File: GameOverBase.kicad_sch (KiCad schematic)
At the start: 55 parts, among them J1 USB_C_DEALON-USB-US31-106, J2 Serial Port, J3 add-on conn, Q1 PMN48XP, SW1 SW_DIP_x08, SW2 boot, SW3 Reset, U1 ESP32-WROOM-E, U2 4021, U3 MCP73831-2ACI-OT, U4 XC6210B332MR

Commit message: Reduces mounting holes to M2 size
It's now clear that this difference will be significant in the layout
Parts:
- H1, H2: footprint MountingHole:MountingHole_3.2mm_M3_DIN965_Pad -> (none)
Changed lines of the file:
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@@
       (effects (font (size 1.27 1.27)) (justify left))
     )
-    (property "Footprint" "MountingHole:MountingHole_3.2mm_M3_DIN965_Pad" (id 2) (at 276.86 142.24 0)
+    (property "Footprint" "" (id 2) (at 276.86 142.24 0)
       (effects (font (size 1.27 1.27)) hide)
     )
@@
       (effects (font (size 1.27 1.27)) (justify left))
     )
-    (property "Footprint" "MountingHole:MountingHole_3.2mm_M3_DIN965_Pad" (id 2) (at 266.7 142.24 0)
+    (property "Footprint" "" (id 2) (at 266.7 142.24 0)
       (effects (font (size 1.27 1.27)) hide)
     )
@@
     )
     (path "/72b8070d-6360-4ae2-9e52-c57614a73147"
-      (reference "H1") (unit 1) (value "~") (footprint "MountingHole:MountingHole_3.2mm_M3_DIN965_Pad")
+      (reference "H1") (unit 1) (value "~") (footprint "MountingHole:MountingHole_2.2mm_M2_Pad_Via")
     )
     (path "/33ba6f87-8078-4806-af25-74c46ae2d6bf"
-      (reference "H2") (unit 1) (value "~") (footprint "MountingHole:MountingHole_3.2mm_M3_DIN965_Pad")
+      (reference "H2") (unit 1) (value "~") (footprint "MountingHole:MountingHole_2.2mm_M2_Pad_Via")
     )
     (path "/c62df308-9d46-4880-b5c7-5b78f375875b"

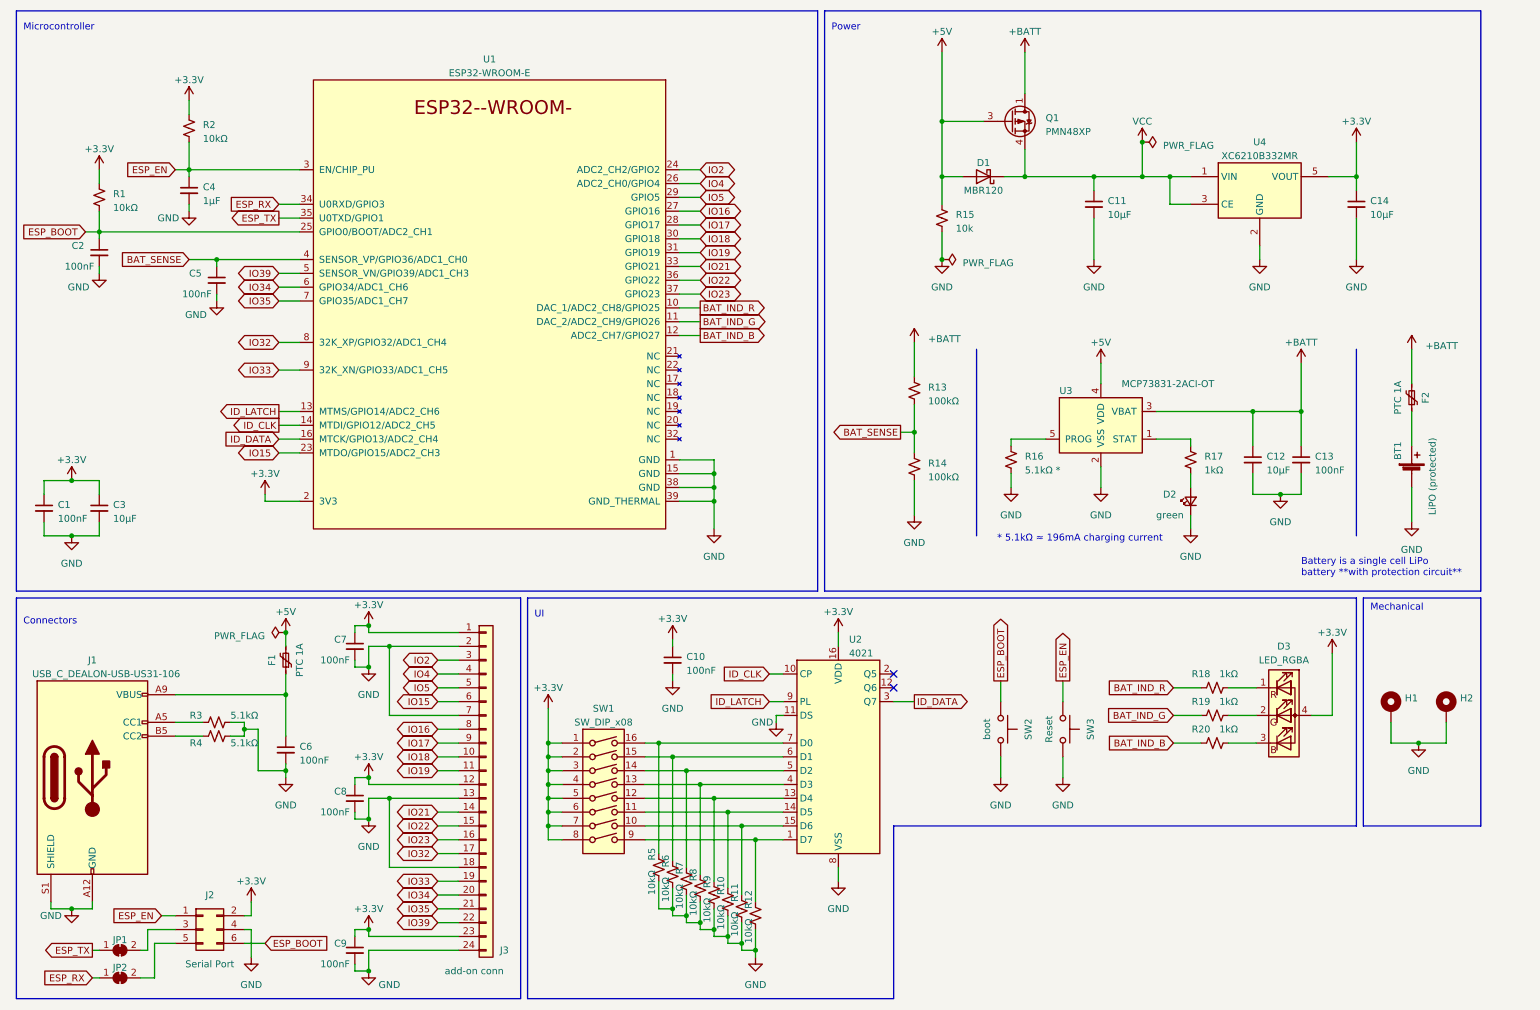
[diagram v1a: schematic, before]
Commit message: Uses a resistor network for the pull-ups in the ID DIP switch
This will save a lot of space on the PCB
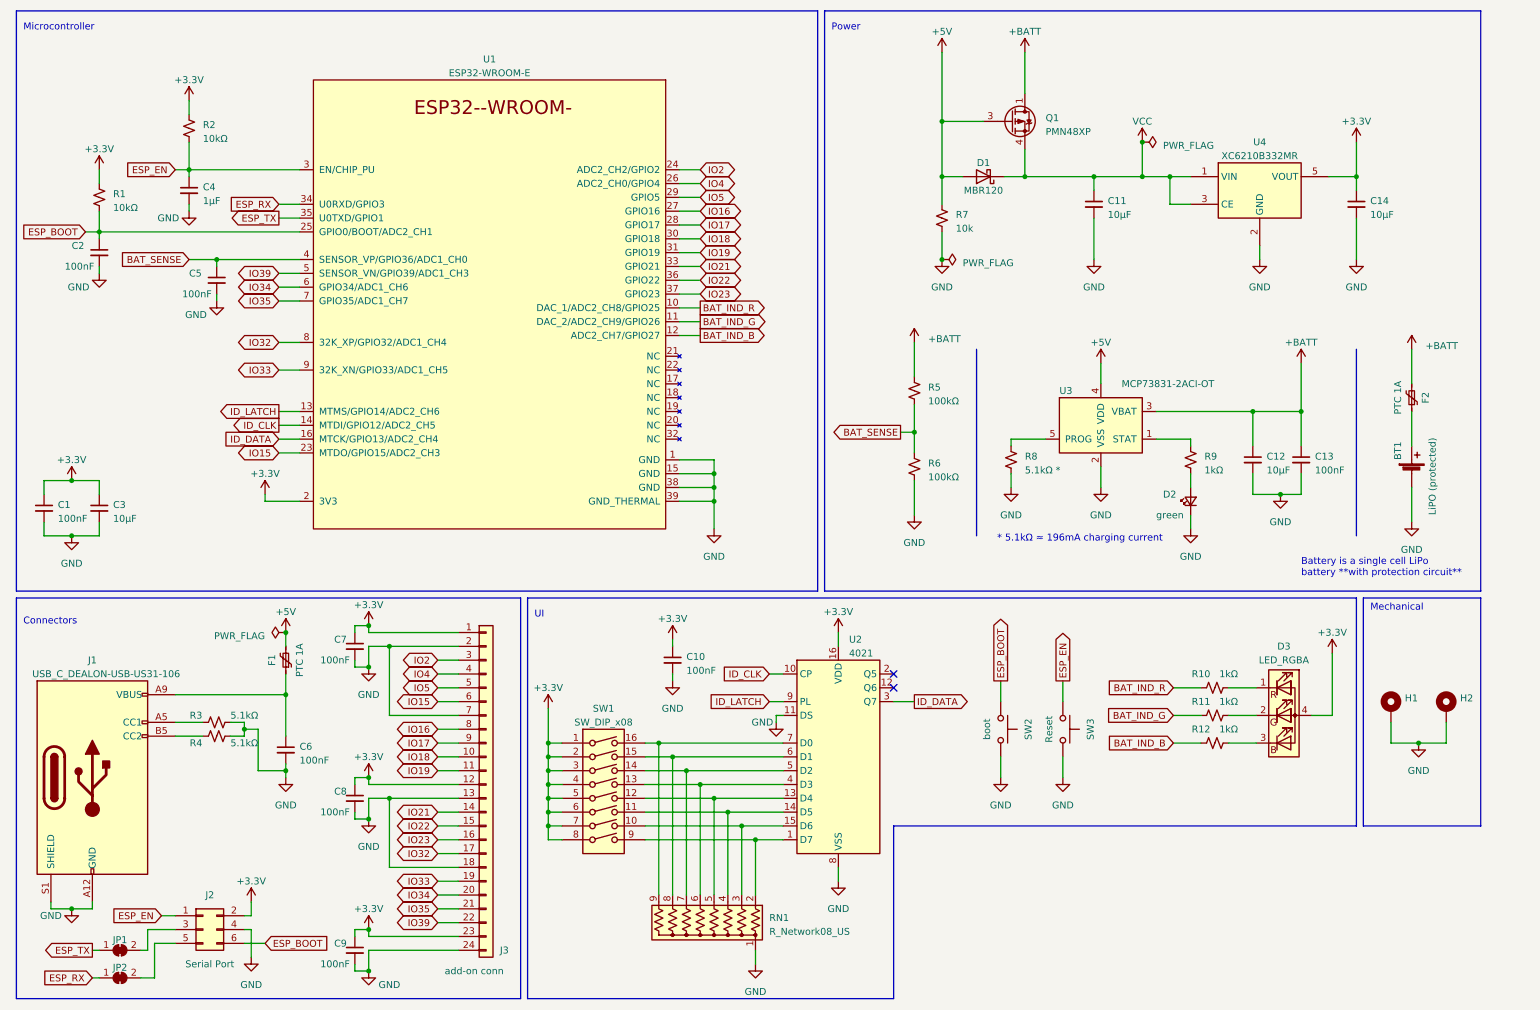
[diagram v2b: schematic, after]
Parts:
- removed R10, R11, R12, R5, R6, R7, R8, R9: 10kΩ, Resistor_SMD:R_0805_2012Metric_Pad1.20x1.40mm_HandSolder, symbol Device:R_Small_US
- added RN1: R_Network08_US, symbol Device:R_Network08_US
- H1, H2: footprint (none) -> MountingHole:MountingHole_2.2mm_M2_Pad_Via
- renumbered R18 to R10, R19 to R11, R20 to R12, R13 to R5, R14 to R6, R15 to R7, R16 to R8, R17 to R9
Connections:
- net GND: now also RN1.1 (common)
- net at SW1.14, U2.5 (D2): now also RN1.7 (R6)
- net at SW1.12, U2.13 (D4): now also RN1.5 (R4)
- net at SW1.9, U2.1 (D7): now also RN1.2 (R1)
- net at SW1.11, U2.14 (D5): now also RN1.4 (R3)
- net at SW1.10, U2.15 (D6): now also RN1.3 (R2)
- net at SW1.13, U2.4 (D3): now also RN1.6 (R5)
- net at SW1.15, U2.6 (D1): now also RN1.8 (R7)
- net at SW1.16, U2.7 (D0): now also RN1.9 (R8)

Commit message: Uses the MCU to check the battery charging status
The STAT pin on the MCP73831 is low when the battery is charging,
high when it's done and hiigh Z when shutdown or the battery is not
present. This means we can read this pin from the microcontroller to
know if the battery is being charged and indicate that using the RGB Led
already present for battery level indication. The pull-up is necessary
since when the charger or battery are not present the pin would be
floating.

We used GPIO39 on the esp32 for this reading, which means this pin is no
longer broken out to the add-on boards. The connector changed to
accomodate for that.
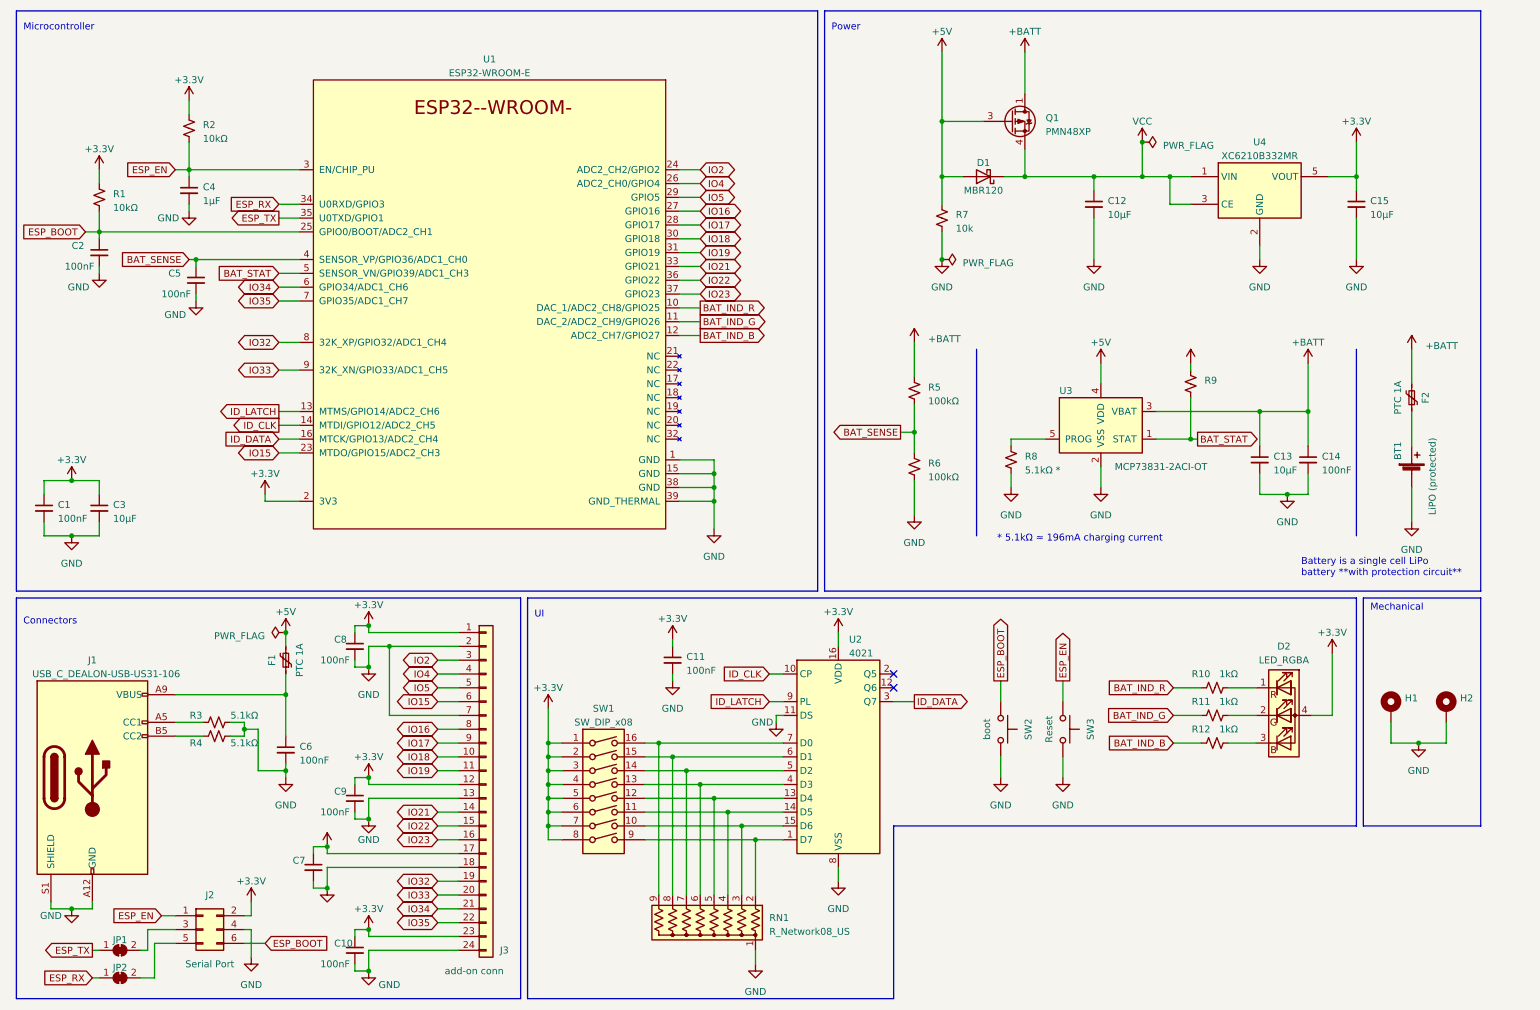
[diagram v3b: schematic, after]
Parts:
- removed D2: green, LED_SMD:LED_0805_2012Metric_Pad1.15x1.40mm_HandSolder, symbol Device:LED_Small
- added C7: (no value), symbol Device:C_Small
- R9: value 1kΩ -> (none)
- RN1: footprint (none) -> Resistor_SMD:R_Array_Convex_5x1206
- renumbered C9 to C10, C10 to C11, C11 to C12, C12 to C13, C13 to C14, C14 to C15, C7 to C8, C8 to C9, D3 to D2
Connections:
- net +3V3: now also J3.17 (Pin_17), R9.1, C7.1
- net GND: now also C7.2
- net IO32: now also J3.19 (Pin_19); no longer J3.17 (Pin_17)
- net IO33: now also J3.20 (Pin_20); no longer J3.19 (Pin_19)
- net IO34: now also J3.21 (Pin_21); no longer J3.20 (Pin_20)
- net IO35: now also J3.22 (Pin_22); no longer J3.21 (Pin_21)
- net BAT_STAT: now reaches U3.1 (STAT)
- net BAT_STAT: now also R9.2, U1.5 (SENSOR_VN/GPIO39/ADC1_CH3); no longer R9.1
- removed net IO39: J3.22 (Pin_22), U1.5 (SENSOR_VN/GPIO39/ADC1_CH3)
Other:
- moved on the sheet: C13, C14, C5, R9

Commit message: Adds extra capacitance to the VBUS decoupling
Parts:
- added C7: 10µF, Capacitor_SMD:C_0805_2012Metric_Pad1.18x1.45mm_HandSolder, symbol Device:C_Small
- C8: renamed from C7; value (none) -> 100nF; footprint (none) -> Capacitor_SMD:C_0805_2012Metric_Pad1.18x1.45mm_HandSolder
- R9: value (none) -> 10kΩ
- renumbered C9 to C10, C10 to C11, C11 to C12, C12 to C13, C13 to C14, C14 to C15, C15 to C16, C8 to C9
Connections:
- net GND: now also C7.2
- net at C6.1, F1.1, J1.A9 (VBUS)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: now also C7.1
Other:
- moved on the sheet: C6, F1, R3, R4

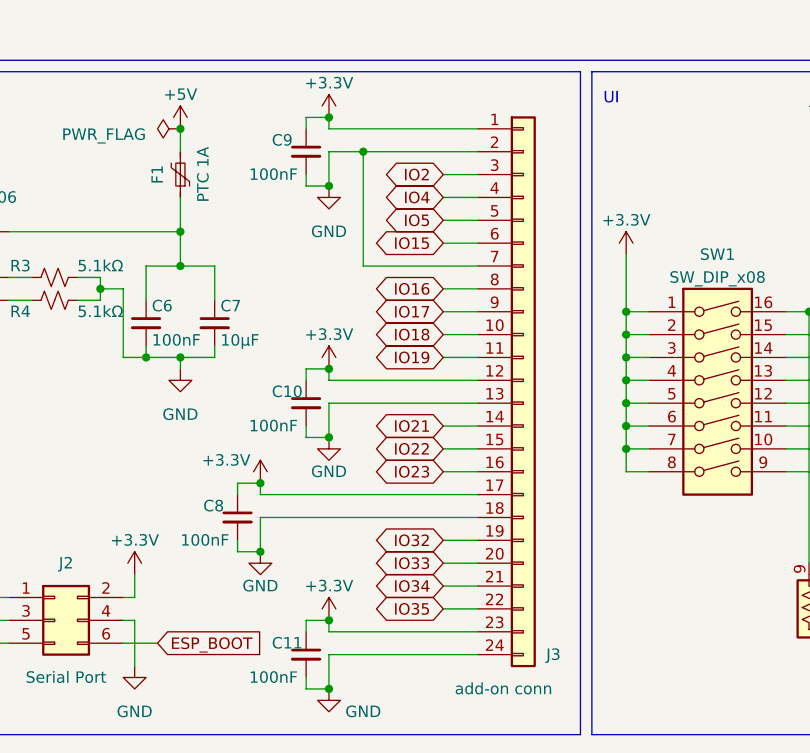
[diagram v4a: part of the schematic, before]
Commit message: Groups ESP32 circuitry and add-on connector
To do this, I reorganized the order the GPIO pins are broken out to the
add-on connector.

This is still missing the decoupling capacitors on the connector
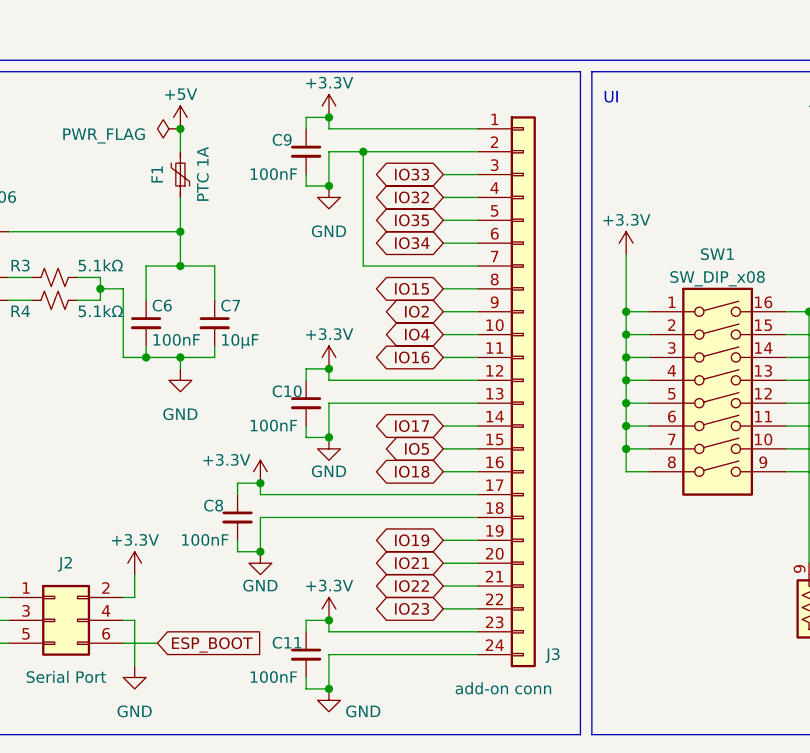
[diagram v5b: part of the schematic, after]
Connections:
- net IO15: now also J3.8 (Pin_8); no longer J3.6 (Pin_6)
- net IO16: now also J3.11 (Pin_11); no longer J3.8 (Pin_8)
- net IO17: now also J3.14 (Pin_14); no longer J3.9 (Pin_9)
- net IO18: now also J3.16 (Pin_16); no longer J3.10 (Pin_10)
- net IO19: now also J3.19 (Pin_19); no longer J3.11 (Pin_11)
- net IO2: now also J3.9 (Pin_9); no longer J3.3 (Pin_3)
- net IO21: now also J3.20 (Pin_20); no longer J3.14 (Pin_14)
- net IO22: now also J3.21 (Pin_21); no longer J3.15 (Pin_15)
- net IO23: now also J3.22 (Pin_22); no longer J3.16 (Pin_16)
- net IO32: now also J3.4 (Pin_4); no longer J3.19 (Pin_19)
- net IO33: now also J3.3 (Pin_3); no longer J3.20 (Pin_20)
- net IO34: now also J3.6 (Pin_6); no longer J3.21 (Pin_21)
- net IO35: now also J3.5 (Pin_5); no longer J3.22 (Pin_22)
- net IO4: now also J3.10 (Pin_10); no longer J3.4 (Pin_4)
- net IO5: now also J3.15 (Pin_15); no longer J3.5 (Pin_5)

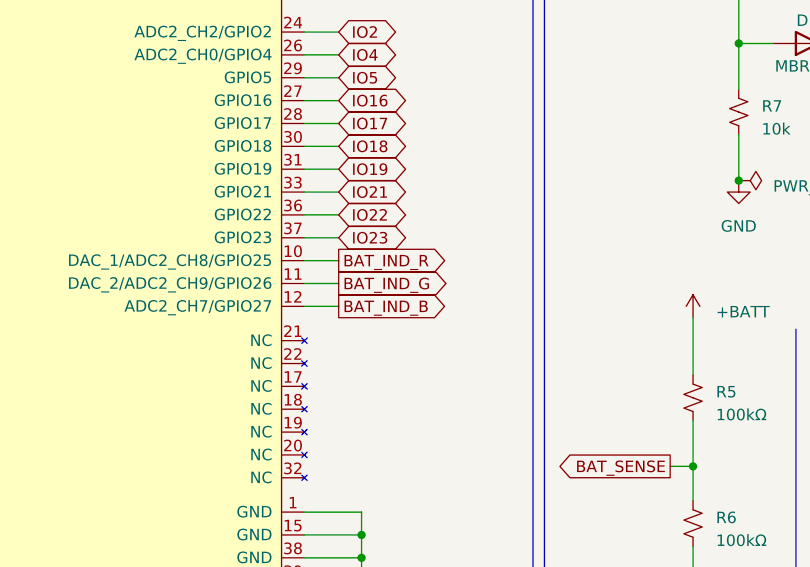
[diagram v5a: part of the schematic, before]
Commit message: Roughly routes buttons and RGB led
To make this routing better I also switched around the GPIO pins for the
RGB leds.
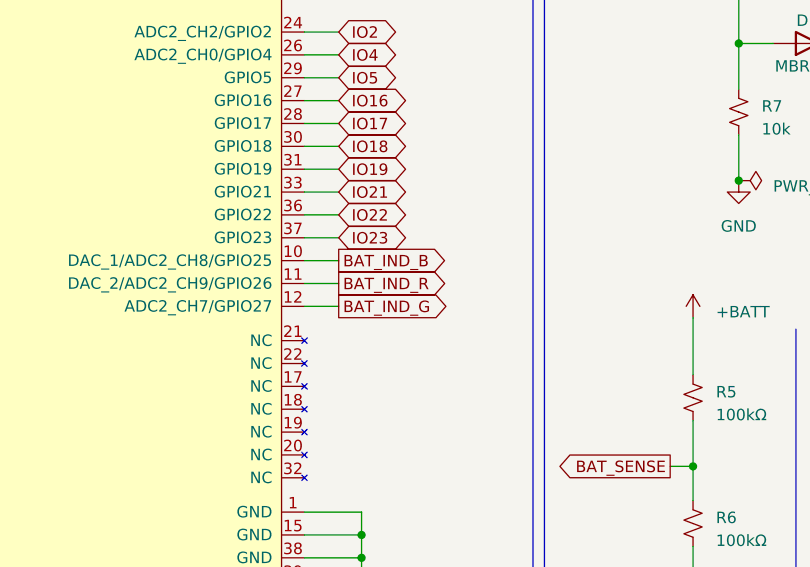
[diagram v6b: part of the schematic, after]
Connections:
- net BAT_IND_B: now also U1.10 (DAC_1/ADC2_CH8/GPIO25); no longer U1.12 (ADC2_CH7/GPIO27)
- net BAT_IND_G: now also U1.12 (ADC2_CH7/GPIO27); no longer U1.11 (DAC_2/ADC2_CH9/GPIO26)
- net BAT_IND_R: now also U1.11 (DAC_2/ADC2_CH9/GPIO26); no longer U1.10 (DAC_1/ADC2_CH8/GPIO25)
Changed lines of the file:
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@@
     )
   )
-  (global_label "BAT_IND_R" (shape output) (at 139.7 68.58 0) (fields_autoplaced)
+  (global_label "BAT_IND_R" (shape output) (at 139.7 71.12 0) (fields_autoplaced)
     (effects (font (size 1.27 1.27)) (justify left))
-    (property "Intersheetrefs" "${INTERSHEET_REFS}" (id 0) (at 152.1837 68.58 0)
+    (property "Intersheetrefs" "${INTERSHEET_REFS}" (id 0) (at 152.1837 71.12 0)
       (effects (font (size 1.27 1.27)) (justify left) hide)
     )
@@
     )
   )
-  (global_label "BAT_IND_G" (shape output) (at 139.7 71.12 0) (fields_autoplaced)
+  (global_label "BAT_IND_G" (shape output) (at 139.7 73.66 0) (fields_autoplaced)
     (effects (font (size 1.27 1.27)) (justify left))
-    (property "Intersheetrefs" "${INTERSHEET_REFS}" (id 0) (at 152.1837 71.12 0)
+    (property "Intersheetrefs" "${INTERSHEET_REFS}" (id 0) (at 152.1837 73.66 0)
       (effects (font (size 1.27 1.27)) (justify left) hide)
     )
@@
     )
   )
-  (global_label "BAT_IND_B" (shape output) (at 139.7 73.66 0) (fields_autoplaced)
+  (global_label "BAT_IND_B" (shape output) (at 139.7 68.58 0) (fields_autoplaced)
     (effects (font (size 1.27 1.27)) (justify left))
-    (property "Intersheetrefs" "${INTERSHEET_REFS}" (id 0) (at 152.1837 73.66 0)
+    (property "Intersheetrefs" "${INTERSHEET_REFS}" (id 0) (at 152.1837 68.58 0)
       (effects (font (size 1.27 1.27)) (justify left) hide)
     )
